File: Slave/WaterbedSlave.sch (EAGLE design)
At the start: 11 parts

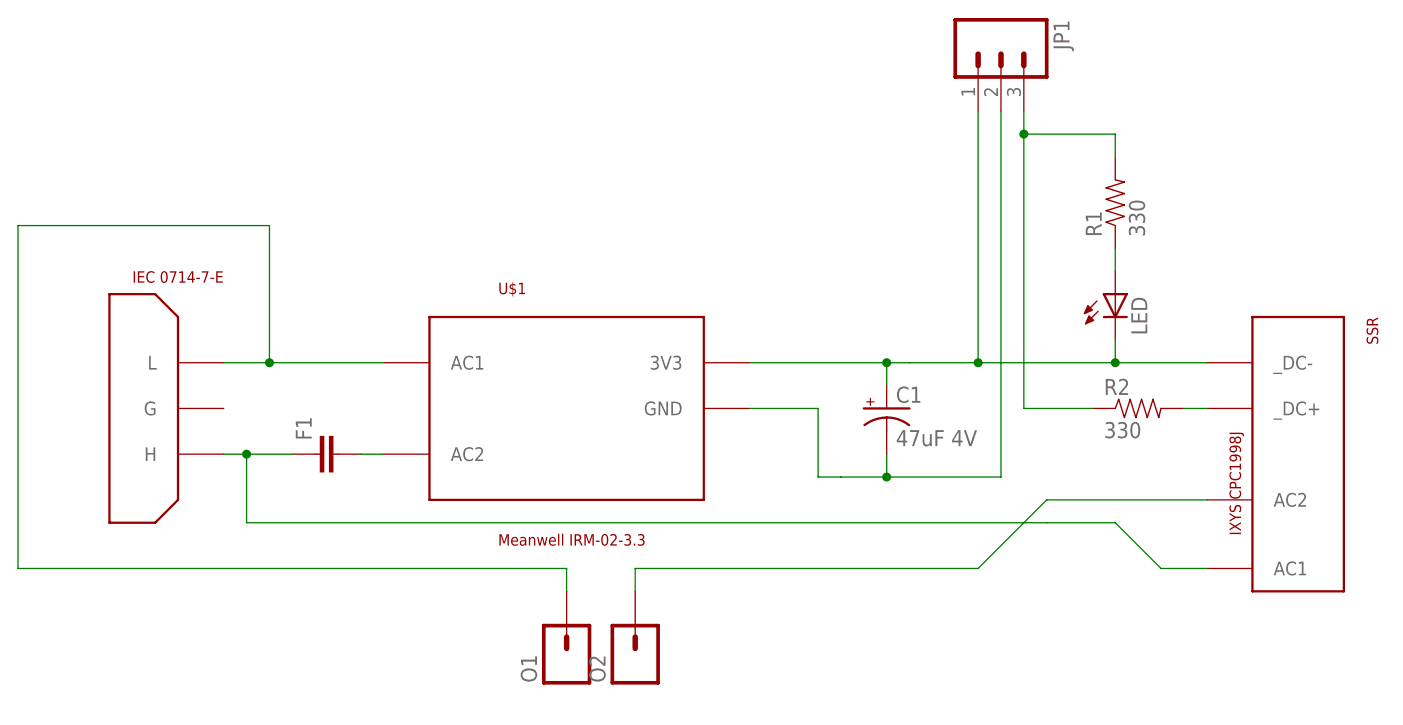
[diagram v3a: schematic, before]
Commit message: Simple 10A 3V relay version
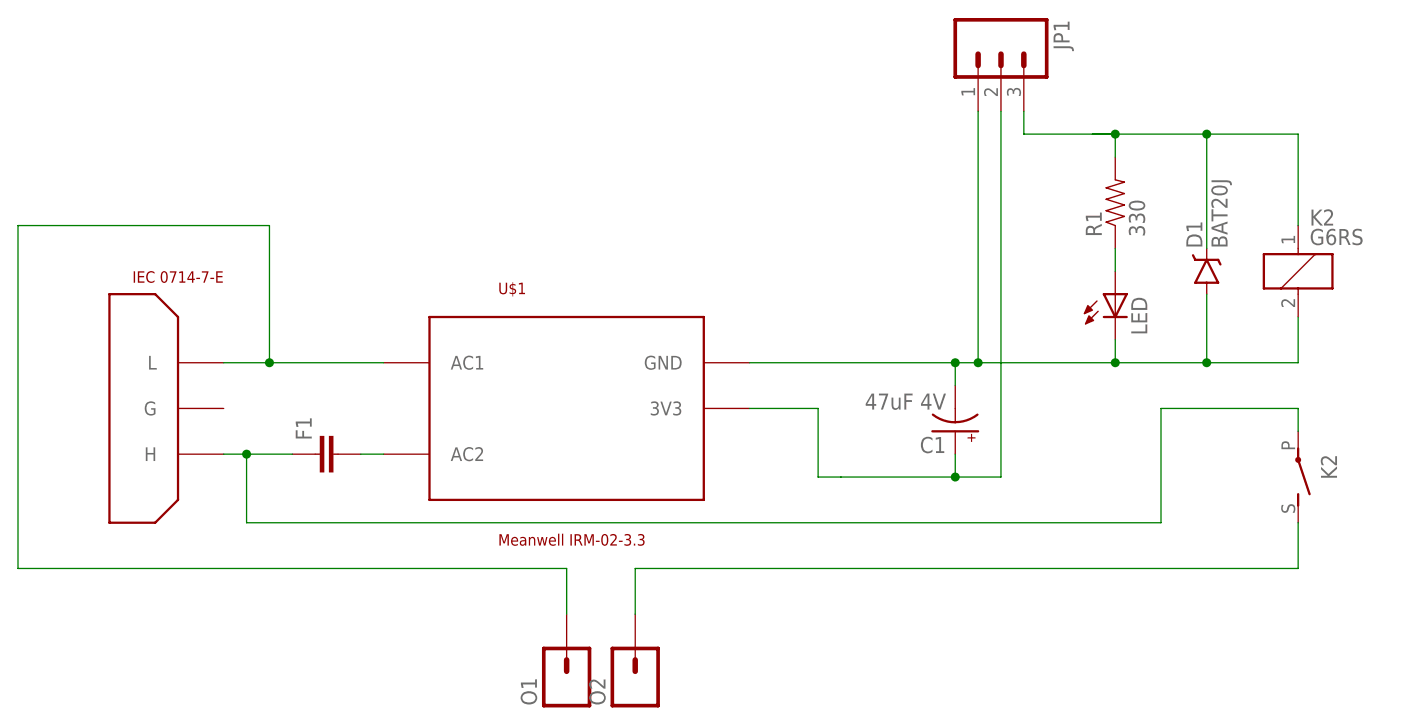
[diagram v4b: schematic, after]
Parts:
- removed R2: 330, SparkFun-Resistors:RESISTOR0805-RES
- removed SSR: IXYS CPC1998J, CuriousTech:SSR-5A-240VACI4-PAC
- added D1: BAT20J, SparkFun-DiscreteSemi:DIODE-SCHOTTKY-BAT20J
- added K2: G6RS, relay:G6RS
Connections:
- removed net N$15: C1.-, JP1.2, U$1.GND
- removed net N$5: R2.2, SSR._DC+
- removed net N$6: F1.1, SSR.AC1, U$3.H
- new net 3V3: C1.+, JP1.2, U$1.3V3
- new net N$4: F1.1, K22.P, U$3.H
- net GND: now also C1.-, D1.A, K21.2, U$1.GND; no longer C1.+, SSR._DC-, U$1.3V3
- net N$16: now also D1.C, K21.1; no longer R2.1
- net N$3: now also K22.S; no longer SSR.AC2
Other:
- moved on the sheet: C1, O1, O2
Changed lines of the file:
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@@
 <?xml version="1.0" encoding="utf-8"?>
 <!DOCTYPE eagle SYSTEM "eagle.dtd">
-<eagle version="9.1.1">
+<eagle version="9.1.3">
 <drawing>
 <settings>
@@
 <part name="LED" library="led" deviceset="LED" device="CHIPLED_0805"/>
 <part name="R1" library="SparkFun-Resistors" deviceset="RESISTOR" device="0805-RES" value="330"/>
-<part name="SSR" library="CuriousTech" deviceset="SSR-5A-240VAC" device="I4-PAC" value="IXYS CPC1998J"/>
-<part name="R2" library="SparkFun-Resistors" deviceset="RESISTOR" device="0805-RES" value="330"/>
 <part name="U$1" library="CuriousTech" deviceset="RAC02-3.3SC" device="" value="Meanwell IRM-02-3.3"/>
 <part name="C1" library="SparkFun-Capacitors" deviceset="CAP_POL" device="PTH2" value="47uF 4V"/>
+<part name="D1" library="SparkFun-DiscreteSemi" deviceset="DIODE-SCHOTTKY" device="-BAT20J" value="BAT20J"/>
+<part name="K2" library="relay" library_urn="urn:adsk.eagle:library:339" deviceset="G6RS" device="" package3d_urn="urn:adsk.eagle:package:24336/1"/>
 </parts>
 <sheets>
@@
 <instance part="JP1" gate="G$1" x="109.22" y="101.6" rot="R270"/>
 <instance part="U$3" gate="G$1" x="17.78" y="55.88" rot="MR180"/>
-<instance part="O1" gate="G$1" x="60.96" y="33.02" rot="R90"/>
-<instance part="O2" gate="G$1" x="68.58" y="33.02" rot="R90"/>
+<instance part="O1" gate="G$1" x="60.96" y="30.48" rot="R90"/>
+<instance part="O2" gate="G$1" x="68.58" y="30.48" rot="R90"/>
 <instance part="F1" gate="G$1" x="35.56" y="55.88" rot="R90"/>
 <instance part="LED" gate="G$1" x="121.92" y="73.66"/>
 <instance part="R1" gate="G$1" x="121.92" y="83.82" rot="R90"/>
-<instance part="SSR" gate="G$1" x="142.24" y="55.88" rot="R270"/>
-<instance part="R2" gate="G$1" x="124.46" y="60.96"/>
 <instance part="U$1" gate="G$1" x="60.96" y="60.96"/>
-<instance part="C1" gate="G$1" x="96.52" y="60.96"/>
+<instance part="C1" gate="G$1" x="104.14" y="58.42" rot="R180"/>
+<instance part="D1" gate="G$1" x="132.08" y="76.2" rot="R90"/>
+<instance part="K2" gate="1" x="142.24" y="76.2"/>
+<instance part="K2" gate="2" x="142.24" y="53.34" rot="R180"/>
 </instances>
 <busses>
@@
 <junction x="106.68" y="66.04"/>
 <wire x1="121.92" y1="66.04" x2="106.68" y2="66.04" width="0.1524" layer="91"/>
-<wire x1="81.28" y1="66.04" x2="96.52" y2="66.04" width="0.1524" layer="91"/>
 <pinref part="LED" gate="G$1" pin="C"/>
-<wire x1="96.52" y1="66.04" x2="99.06" y2="66.04" width="0.1524" layer="91"/>
-<wire x1="99.06" y1="66.04" x2="106.68" y2="66.04" width="0.1524" layer="91"/>
+<wire x1="104.14" y1="63.5" x2="104.14" y2="66.04" width="0.1524" layer="91"/>
+<wire x1="104.14" y1="66.04" x2="106.68" y2="66.04" width="0.1524" layer="91"/>
 <wire x1="121.92" y1="68.58" x2="121.92" y2="66.04" width="0.1524" layer="91"/>
 <wire x1="121.92" y1="66.04" x2="132.08" y2="66.04" width="0.1524" layer="91"/>
 <junction x="121.92" y="66.04"/>
-<pinref part="SSR" gate="G$1" pin="_DC-"/>
-<pinref part="U$1" gate="G$1" pin="3V3"/>
-<pinref part="C1" gate="G$1" pin="+"/>
-<wire x1="96.52" y1="63.5" x2="96.52" y2="66.04" width="0.1524" layer="91"/>
-<junction x="96.52" y="66.04"/>
-</segment>
-</net>
-<net name="N$15" class="0">
-<segment>
-<wire x1="81.28" y1="60.96" x2="88.9" y2="60.96" width="0.1524" layer="91"/>
+<wire x1="132.08" y1="66.04" x2="142.24" y2="66.04" width="0.1524" layer="91"/>
+<pinref part="D1" gate="G$1" pin="A"/>
+<wire x1="132.08" y1="73.66" x2="132.08" y2="66.04" width="0.1524" layer="91"/>
+<junction x="132.08" y="66.04"/>
+<pinref part="C1" gate="G$1" pin="-"/>
+<junction x="104.14" y="66.04"/>
+<wire x1="142.24" y1="71.12" x2="142.24" y2="66.04" width="0.1524" layer="91"/>
+<pinref part="U$1" gate="G$1" pin="GND"/>
+<wire x1="81.28" y1="66.04" x2="104.14" y2="66.04" width="0.1524" layer="91"/>
+<pinref part="K2" gate="1" pin="2"/>
+</segment>
+</net>
+<net name="3V3" class="0">
+<segment>
 <pinref part="JP1" gate="G$1" pin="2"/>
 <wire x1="88.9" y1="60.96" x2="88.9" y2="53.34" width="0.1524" layer="91"/>
 <wire x1="88.9" y1="53.34" x2="91.44" y2="53.34" width="0.1524" layer="91"/>
-<wire x1="91.44" y1="53.34" x2="96.52" y2="53.34" width="0.1524" layer="91"/>
-<wire x1="96.52" y1="53.34" x2="109.22" y2="53.34" width="0.1524" layer="91"/>
+<wire x1="91.44" y1="53.34" x2="104.14" y2="53.34" width="0.1524" layer="91"/>
+<wire x1="104.14" y1="53.34" x2="109.22" y2="53.34" width="0.1524" layer="91"/>
 <wire x1="109.22" y1="53.34" x2="109.22" y2="93.98" width="0.1524" layer="91"/>
-<pinref part="U$1" gate="G$1" pin="GND"/>
-<pinref part="C1" gate="G$1" pin="-"/>
-<wire x1="96.52" y1="55.88" x2="96.52" y2="53.34" width="0.1524" layer="91"/>
-<junction x="96.52" y="53.34"/>
+<pinref part="C1" gate="G$1" pin="+"/>
+<wire x1="104.14" y1="55.88" x2="104.14" y2="53.34" width="0.1524" layer="91"/>
+<junction x="104.14" y="53.34"/>
+<pinref part="U$1" gate="G$1" pin="3V3"/>
+<wire x1="81.28" y1="60.96" x2="88.9" y2="60.96" width="0.1524" layer="91"/>
 </segment>
 </net>
@@
 <pinref part="JP1" gate="G$1" pin="3"/>
 <wire x1="111.76" y1="93.98" x2="111.76" y2="91.44" width="0.1524" layer="91"/>
-<wire x1="111.76" y1="91.44" x2="111.76" y2="60.96" width="0.1524" layer="91"/>
+<wire x1="111.76" y1="91.44" x2="121.92" y2="91.44" width="0.1524" layer="91"/>
 <pinref part="R1" gate="G$1" pin="2"/>
 <wire x1="121.92" y1="88.9" x2="121.92" y2="91.44" width="0.1524" layer="91"/>
-<wire x1="121.92" y1="91.44" x2="111.76" y2="91.44" width="0.1524" layer="91"/>
-<junction x="111.76" y="91.44"/>
-<pinref part="R2" gate="G$1" pin="1"/>
-<wire x1="111.76" y1="60.96" x2="119.38" y2="60.96" width="0.1524" layer="91"/>
+<wire x1="121.92" y1="91.44" x2="119.38" y2="91.44" width="0.1524" layer="91"/>
+<wire x1="121.92" y1="91.44" x2="132.08" y2="91.44" width="0.1524" layer="91"/>
+<pinref part="D1" gate="G$1" pin="C"/>
+<wire x1="132.08" y1="91.44" x2="142.24" y2="91.44" width="0.1524" layer="91"/>
+<wire x1="132.08" y1="91.44" x2="132.08" y2="78.74" width="0.1524" layer="91"/>
+<junction x="132.08" y="91.44"/>
+<junction x="121.92" y="91.44"/>
+<wire x1="142.24" y1="81.28" x2="142.24" y2="91.44" width="0.1524" layer="91"/>
+<pinref part="K2" gate="1" pin="1"/>
 </segment>
 </net>
@@
 <pinref part="U$3" gate="G$1" pin="L"/>
 <wire x1="22.86" y1="66.04" x2="27.94" y2="66.04" width="0.1524" layer="91"/>
-<wire x1="60.96" y1="40.64" x2="60.96" y2="43.18" width="0.1524" layer="91"/>
+<wire x1="60.96" y1="38.1" x2="60.96" y2="43.18" width="0.1524" layer="91"/>
 <wire x1="60.96" y1="43.18" x2="0" y2="43.18" width="0.1524" layer="91"/>
 <wire x1="0" y1="43.18" x2="0" y2="81.28" width="0.1524" layer="91"/>
@@
 <net name="N$3" class="0">
 <segment>
-<wire x1="68.58" y1="43.18" x2="68.58" y2="40.64" width="0.1524" layer="91"/>
+<wire x1="68.58" y1="43.18" x2="68.58" y2="38.1" width="0.1524" layer="91"/>
 <pinref part="O2" gate="G$1" pin="1"/>
-<wire x1="68.58" y1="43.18" x2="106.68" y2="43.18" width="0.1524" layer="91"/>
-<wire x1="106.68" y1="43.18" x2="114.3" y2="50.8" width="0.1524" layer="91"/>
-<pinref part="SSR" gate="G$1" pin="AC2"/>
-<wire x1="114.3" y1="50.8" x2="132.08" y2="50.8" width="0.1524" layer="91"/>
-</segment>
-</net>
-<net name="N$6" class="0">
+<wire x1="68.58" y1="43.18" x2="142.24" y2="43.18" width="0.1524" layer="91"/>
+<pinref part="K2" gate="2" pin="S"/>
+<wire x1="142.24" y1="48.26" x2="142.24" y2="43.18" width="0.1524" layer="91"/>
+</segment>
+</net>
+<net name="N$4" class="0">
 <segment>
 <wire x1="25.4" y1="55.88" x2="25.4" y2="48.26" width="0.1524" layer="91"/>
-<wire x1="25.4" y1="48.26" x2="114.3" y2="48.26" width="0.1524" layer="91"/>
+<wire x1="25.4" y1="48.26" x2="127" y2="48.26" width="0.1524" layer="91"/>
 <pinref part="U$3" gate="G$1" pin="H"/>
 <wire x1="22.86" y1="55.88" x2="25.4" y2="55.88" width="0.1524" layer="91"/>
@@
 <wire x1="25.4" y1="55.88" x2="30.48" y2="55.88" width="0.1524" layer="91"/>
 <junction x="25.4" y="55.88"/>
-<wire x1="114.3" y1="48.26" x2="121.92" y2="48.26" width="0.1524" layer="91"/>
-<wire x1="121.92" y1="48.26" x2="127" y2="43.18" width="0.1524" layer="91"/>
-<wire x1="129.54" y1="43.18" x2="132.08" y2="43.18" width="0.1524" layer="91"/>
-<pinref part="SSR" gate="G$1" pin="AC1"/>
-<wire x1="127" y1="43.18" x2="129.54" y2="43.18" width="0.1524" layer="91"/>
-</segment>
-</net>
-<net name="N$5" class="0">
-<segment>
-<pinref part="SSR" gate="G$1" pin="_DC+"/>
-<wire x1="129.54" y1="60.96" x2="132.08" y2="60.96" width="0.1524" layer="91"/>
-<pinref part="R2" gate="G$1" pin="2"/>
+<wire x1="127" y1="48.26" x2="127" y2="60.96" width="0.1524" layer="91"/>
+<wire x1="127" y1="60.96" x2="142.24" y2="60.96" width="0.1524" layer="91"/>
+<pinref part="K2" gate="2" pin="P"/>
+<wire x1="142.24" y1="58.42" x2="142.24" y2="60.96" width="0.1524" layer="91"/>
 </segment>
 </net>
@@
 </schematic>
 </drawing>
+<compatibility>
+<note version="8.2" severity="warning">
+Since Version 8.2, EAGLE supports online libraries. The ids
+of those online libraries will not be understood (or retained)
+with this version.
+</note>
+<note version="8.3" severity="warning">
+Since Version 8.3, EAGLE supports URNs for individual library
+assets (packages, symbols, and devices). The URNs of those assets
+will not be understood (or retained) with this version.
+</note>
+<note version="8.3" severity="warning">
+Since Version 8.3, EAGLE supports the association of 3D packages
+with devices in libraries, schematics, and board files. Those 3D
+packages will not be understood (or retained) with this version.
+</note>
+</compatibility>
 </eagle>
